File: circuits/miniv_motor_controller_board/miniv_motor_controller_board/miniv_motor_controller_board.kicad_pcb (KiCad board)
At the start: 2 copper layers, 25 parts, among them J1 DC_in, J2 T200_ESC_power, J3 T200_ESC_signal, J4 Conn_EStop_Signal, Q1 2SC1815, Q2 2SC1815, U1 Teensy4.1, U2 TLP624, U3 TLP624

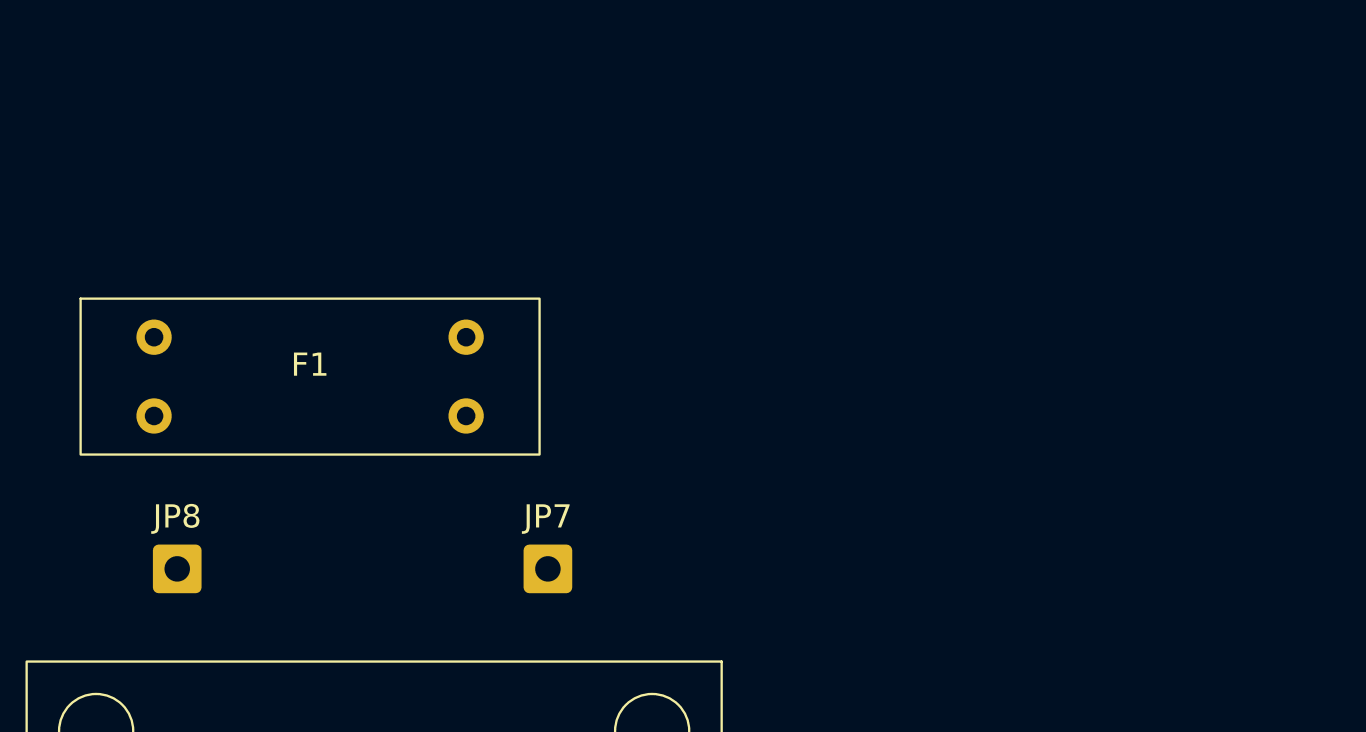
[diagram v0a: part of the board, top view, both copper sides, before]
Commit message: fix connection
Signed-off-by: Masaya Kataoka <ms.kataoka@gmail.com>
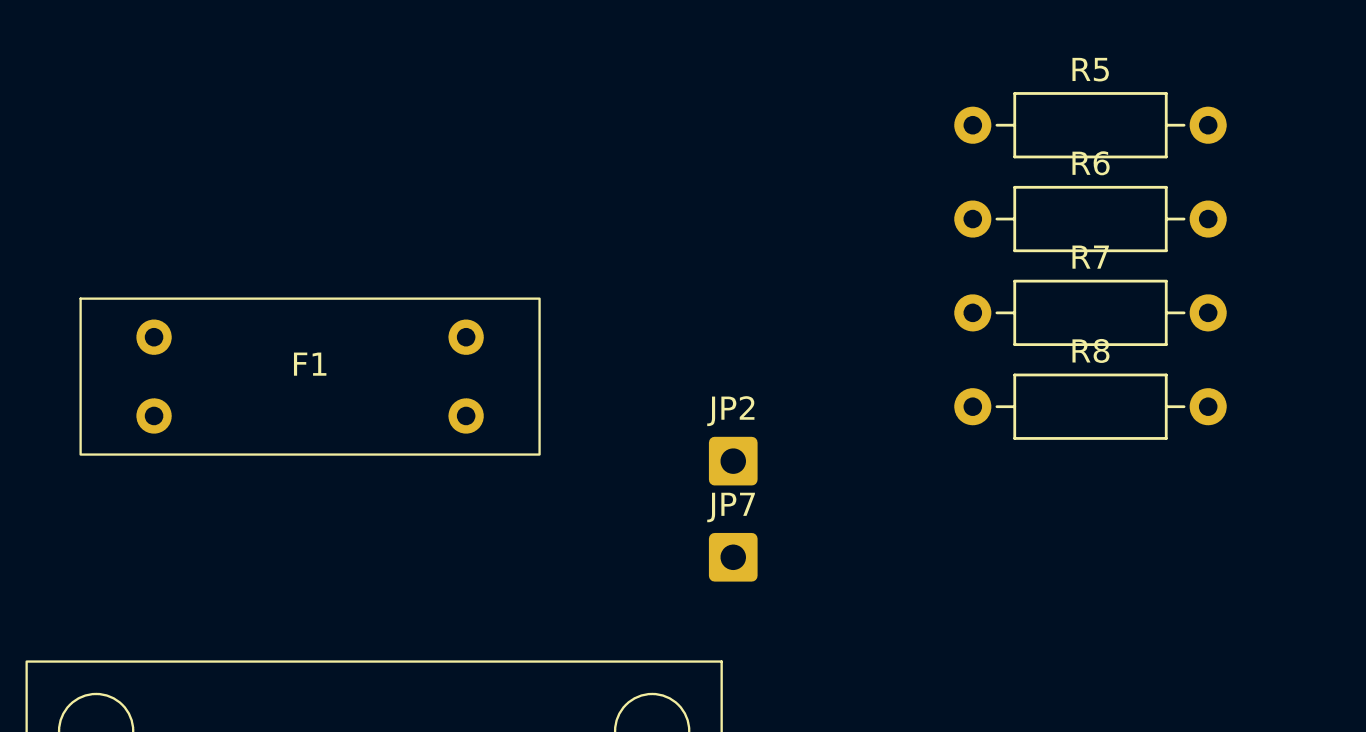
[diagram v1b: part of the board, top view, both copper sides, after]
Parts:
- removed JP8: Jumper_2_Bridged, Connector_Wire:SolderWire-0.5sqmm_1x01_D0.9mm_OD2.1mm
- added JP2: Jumper_2_Bridged, Connector_Wire:SolderWire-0.5sqmm_1x01_D0.9mm_OD2.1mm, F.Cu at (93.0, 48.4)
- added R5: 390, Resistor_THT:R_Axial_DIN0207_L6.3mm_D2.5mm_P10.16mm_Horizontal, F.Cu at (103.3, 33.9)
- added R6: 1K, Resistor_THT:R_Axial_DIN0207_L6.3mm_D2.5mm_P10.16mm_Horizontal, F.Cu at (103.3, 37.9)
- added R7: 1K, Resistor_THT:R_Axial_DIN0207_L6.3mm_D2.5mm_P10.16mm_Horizontal, F.Cu at (103.3, 42.0)
- added R8: 390, Resistor_THT:R_Axial_DIN0207_L6.3mm_D2.5mm_P10.16mm_Horizontal, F.Cu at (103.3, 46.0)
- moved JP7 8.02 mm to (93.0, 52.5)
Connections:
- JP7 pad 1: Net-(JP7-A) -> GND
- U1 pad 45: Net-(U1-23_A9_CRX1_MCLK1) -> Net-(JP1-A)
- U2 pad 1: Net-(JP1-A) -> Net-(R5-Pad2)
- U3 pad 1: Net-(J4-Pin_2) -> Net-(R7-Pad1)
- U3 pad 4: Net-(JP3-B) -> Net-(JP3-A)

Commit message: update text
Signed-off-by: Masaya Kataoka <ms.kataoka@gmail.com>
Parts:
- moved JP7 24.5 mm to (68.5, 53.0)
- moved JP2 12.4 mm to (81.5, 53.0)
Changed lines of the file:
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@@
 	(footprint "Connector_Wire:SolderWire-0.5sqmm_1x01_D0.9mm_OD2.1mm"
 		(layer "F.Cu")
-		(at 93 52.5)
+		(at 68.5 53)
 		(descr "Soldered wire connection, for a single 0.5 mm² wire, basic insulation, conductor diameter 0.9mm, outer diameter 2.1mm, size source Multi-Contact FLEXI-E 0.5 (https://ec.staubli.com/AcroFiles/Catalogues/TM_Cab-Main-11014119_(en)_hi.pdf), bend radius 3 times outer diameter, generated with kicad-footprint-generator")
 		(tags "connector wire 0.5sqmm")
@@
 	(footprint "Connector_Wire:SolderWire-0.5sqmm_1x01_D0.9mm_OD2.1mm"
 		(layer "F.Cu")
-		(at 93 48.35)
+		(at 81.5 53)
 		(descr "Soldered wire connection, for a single 0.5 mm² wire, basic insulation, conductor diameter 0.9mm, outer diameter 2.1mm, size source Multi-Contact FLEXI-E 0.5 (https://ec.staubli.com/AcroFiles/Catalogues/TM_Cab-Main-11014119_(en)_hi.pdf), bend radius 3 times outer diameter, generated with kicad-footprint-generator")
 		(tags "connector wire 0.5sqmm")

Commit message: add hole
Signed-off-by: Masaya Kataoka <ms.kataoka@gmail.com>
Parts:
- removed the R5 at (103.3, 33.9)
- removed the R5 at (102.5, 75.0)
- added H1: MountingHole, MountingHole:MountingHole_3.2mm_M3, F.Cu at (35.0, 130.0)
- added H2: MountingHole, MountingHole:MountingHole_3.2mm_M3, F.Cu at (35.0, 39.0)
- added H3: MountingHole, MountingHole:MountingHole_3.2mm_M3, F.Cu at (104.0, 39.0)
- added H4: MountingHole, MountingHole:MountingHole_3.2mm_M3, F.Cu at (104.0, 130.0)
- added R5: 390, Resistor_THT:R_Axial_DIN0207_L6.3mm_D2.5mm_P10.16mm_Horizontal, F.Cu at (95.5, 107.5)
- J1, J2: footprint Connector_AMASS:AMASS_XT30PW-F_1x02_P2.50mm_Horizontal -> Connector_AMASS:AMASS_XT60PW-F_1x02_P7.20mm_Horizontal
- J4: footprint Connector_AMASS:AMASS_XT30PW-F_1x02_P2.50mm_Horizontal -> Connector_JST:JST_XH_B2B-XH-A_1x02_P2.50mm_Vertical
- JP2: value Jumper_2_Bridged -> Relay_NO
- JP3: value Jumper_EStop -> Disable_EStop
- JP4: value Jumper_2_Bridged -> Relay_SIG
- JP5: value Jumper_2_Bridged -> Relay_GND
- JP6: value Jumper_2_Bridged -> Relay_VCC
- JP7: value Jumper_2_Bridged -> Relay_COM
- moved R7 100.4 mm to (33.5, 114.1), turned to 90 degrees
- moved R8 89.0 mm to (33.5, 101.2), turned to 90 degrees
- moved R6 56.6 mm to (95.5, 93.9), turned to -90 degrees
- moved D2 56.3 mm to (79.0, 120.0), turned to 0 degrees
- moved J1 46.0 mm to (37.5, 70.5)
- moved J3 45.2 mm to (92.0, 51.6), turned to 0 degrees
- moved JP7 44.9 mm to (38.0, 86.0)
- moved JP6 32.9 mm to (38.0, 101.0)
- moved R4 30.4 mm to (84.0, 120.0), turned to 0 degrees
- moved R2 20.4 mm to (98.0, 122.1), turned to 90 degrees
- moved R3 19.7 mm to (83.9, 125.0)
- moved M78AR05-1 19.3 mm to (70.0, 121.0), turned to 180 degrees
- moved R1 14.1 mm to (75.5, 132.5)
- moved Q1 13.8 mm to (81.0, 129.5)
- moved Q2 13.8 mm to (88.5, 129.5)
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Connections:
- JP7 pad 1: GND -> +12V
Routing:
- net GND: track 0.00 -> 239.5 mm
- net Net-(JP3-A): track 0.00 -> 107.8 mm
- net +12V: track 0.00 -> 79.8 mm
- net Net-(JP1-A): track 0.00 -> 64.6 mm
- net Net-(JP3-B): track 0.00 -> 55.0 mm
- net Net-(J2-Pin_2): track 0.00 -> 35.8 mm
- net Net-(JP4-A): track 0.00 -> 34.5 mm
- net Net-(J4-Pin_2): track 0.00 -> 33.1 mm
- net Net-(J3-Pin_2): track 0.00 -> 29.7 mm
- net Net-(R5-Pad2): track 0.00 -> 29.3 mm
- net Net-(R7-Pad1): track 0.00 -> 22.3 mm
- net Net-(Q2-B): track 0.00 -> 14.4 mm
- net Net-(R1-Pad2): track 0.00 -> 14.3 mm
- net Net-(J4-Pin_1): track 0.00 -> 13.3 mm
- net Net-(Q1-B): track 0.00 -> 5.71 mm
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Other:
- board outline added: 78 x 102 mm

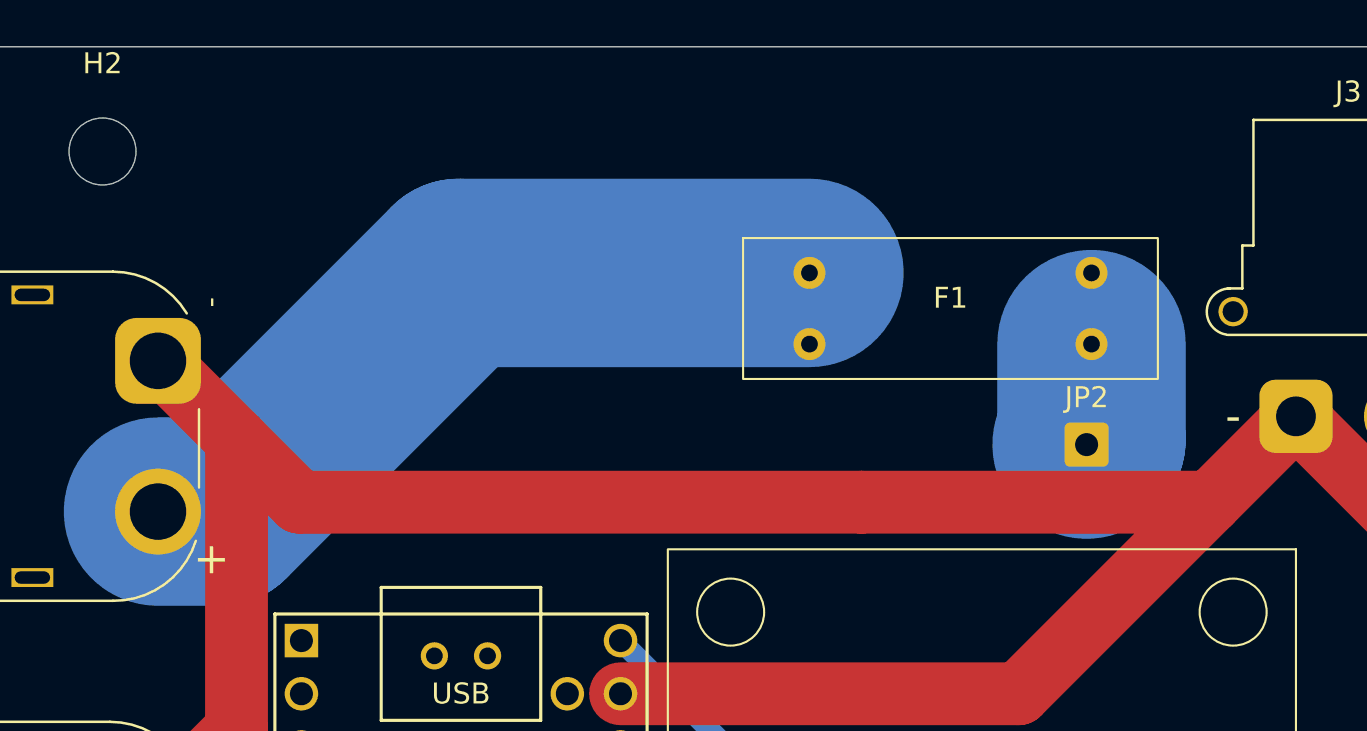
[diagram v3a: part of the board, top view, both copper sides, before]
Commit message: add RJ45 connector
Signed-off-by: Masaya Kataoka <ms.kataoka@gmail.com>
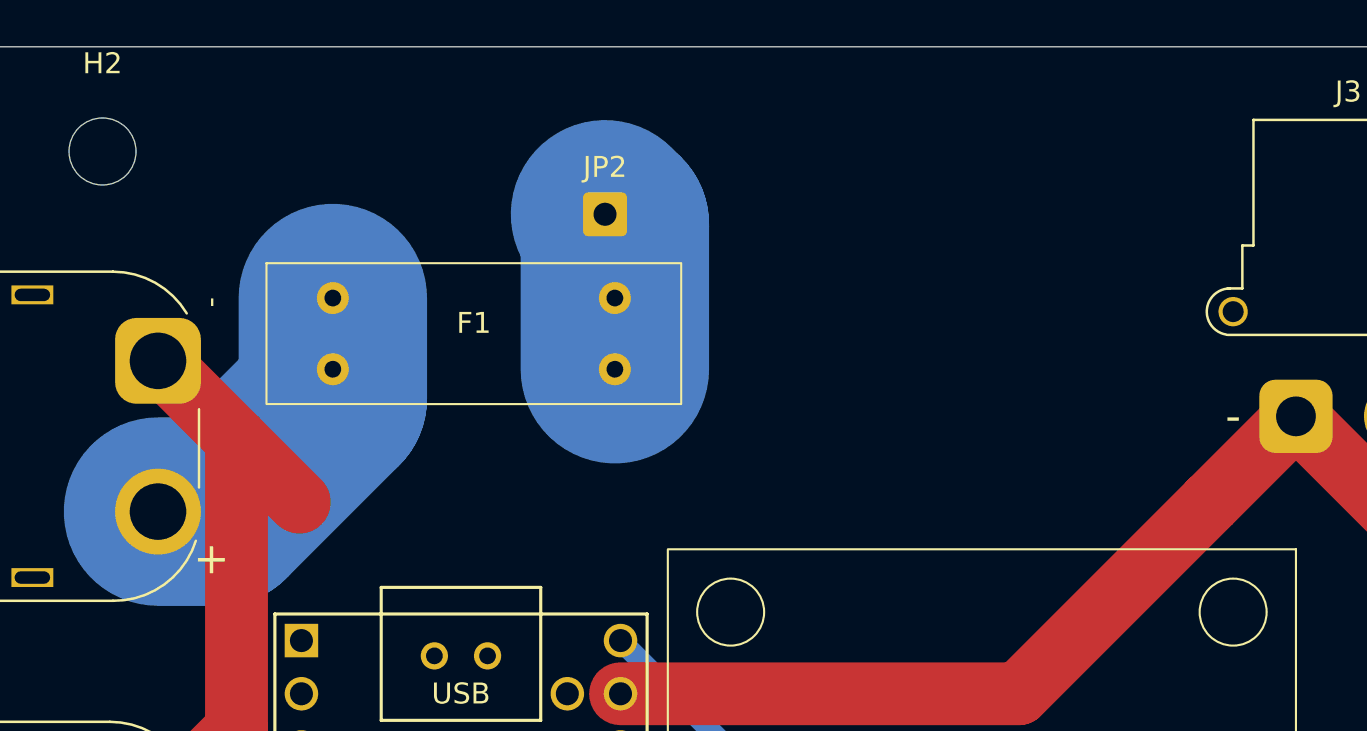
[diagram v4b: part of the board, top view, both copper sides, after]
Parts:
- moved JP2 25.5 mm to (59.0, 42.0)
- moved F1 22.8 mm to (52.7, 47.7)
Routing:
- net GND: track 239.5 -> 196.0 mm
- net Net-(J2-Pin_2): track 35.8 -> 15.4 mm
- net Net-(JP2-A): track 4.90 -> 7.59 mm
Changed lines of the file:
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@@
 		(tags "Resistor Axial_DIN0207 series Axial Horizontal pin pitch 10.16mm 0.25W = 1/4W length 6.3mm diameter 2.5mm")
 		(property "Reference" "R4"
-			(at 8.08 2.5 360)
+			(at 8.08 2.5 0)
 			(layer "F.SilkS")
 			(effects
@@
 		)
 		(property "Value" "470"
-			(at 5.08 2.37 360)
+			(at 5.08 2.37 0)
 			(layer "F.Fab")
 			(effects
@@
 		)
 		(fp_text user "${REFERENCE}"
-			(at 5.08 0 360)
+			(at 5.08 0 0)
 			(layer "F.Fab")
 			(effects
@@
 	(footprint "Connector_Wire:SolderWire-0.5sqmm_1x01_D0.9mm_OD2.1mm"
 		(layer "F.Cu")
-		(at 82 53)
+		(at 59 42)
 		(descr "Soldered wire connection, for a single 0.5 mm² wire, basic insulation, conductor diameter 0.9mm, outer diameter 2.1mm, size source Multi-Contact FLEXI-E 0.5 (https://ec.staubli.com/AcroFiles/Catalogues/TM_Cab-Main-11014119_(en)_hi.pdf), bend radius 3 times outer diameter, generated with kicad-footprint-generator")
 		(tags "connector wire 0.5sqmm")
@@
 	(footprint "3557-15:3557-15"
 		(layer "F.Cu")
-		(at 75.5 46.5)
+		(at 52.735 47.7)
 		(property "Reference" "F1"
 			(at 0 -0.5 0)
@@
 	)
 	(segment
-		(start 71.25 55.75)
-		(end 44.4 55.75)
-		(width 3)
-		(layer "F.Cu")
-		(net 2)
-	)
-	(segment
 		(start 83.92 124.92)
 		(end 79 120)
@@
 	)
 	(segment
-		(start 71.25 55.75)
-		(end 87.9 55.75)
-		(width 3)
-		(layer "F.Cu")
-		(net 2)
-	)
-	(segment
 		(start 44.4 55.75)
 		(end 41.4 52.75)
@@
 	)
 	(segment
-		(start 68.765 44.8)
-		(end 52.003388 44.8)
+		(start 40.603388 56.2)
+		(end 37.65 56.2)
 		(width 9)
 		(layer "B.Cu")
@@
 	)
 	(segment
-		(start 40.603388 56.2)
-		(end 37.65 56.2)
+		(start 46 50.803388)
+		(end 46 46)
 		(width 9)
 		(layer "B.Cu")
@@
 	)
 	(segment
-		(start 52.003388 44.8)
-		(end 40.603388 56.2)
+		(start 40.603388 56.2)
+		(end 46 50.803388)
 		(width 9)
 		(layer "B.Cu")
@@
 	)
 	(segment
-		(start 82.235 48.2)
-		(end 82.235 52.765)
+		(start 59.47 49.4)
+		(end 59.47 42.47)
 		(width 9)
 		(layer "B.Cu")
@@
 	)
 	(segment
-		(start 82.235 52.765)
-		(end 82 53)
+		(start 59.47 42.47)
+		(end 59 42)
 		(width 9)
 		(layer "B.Cu")

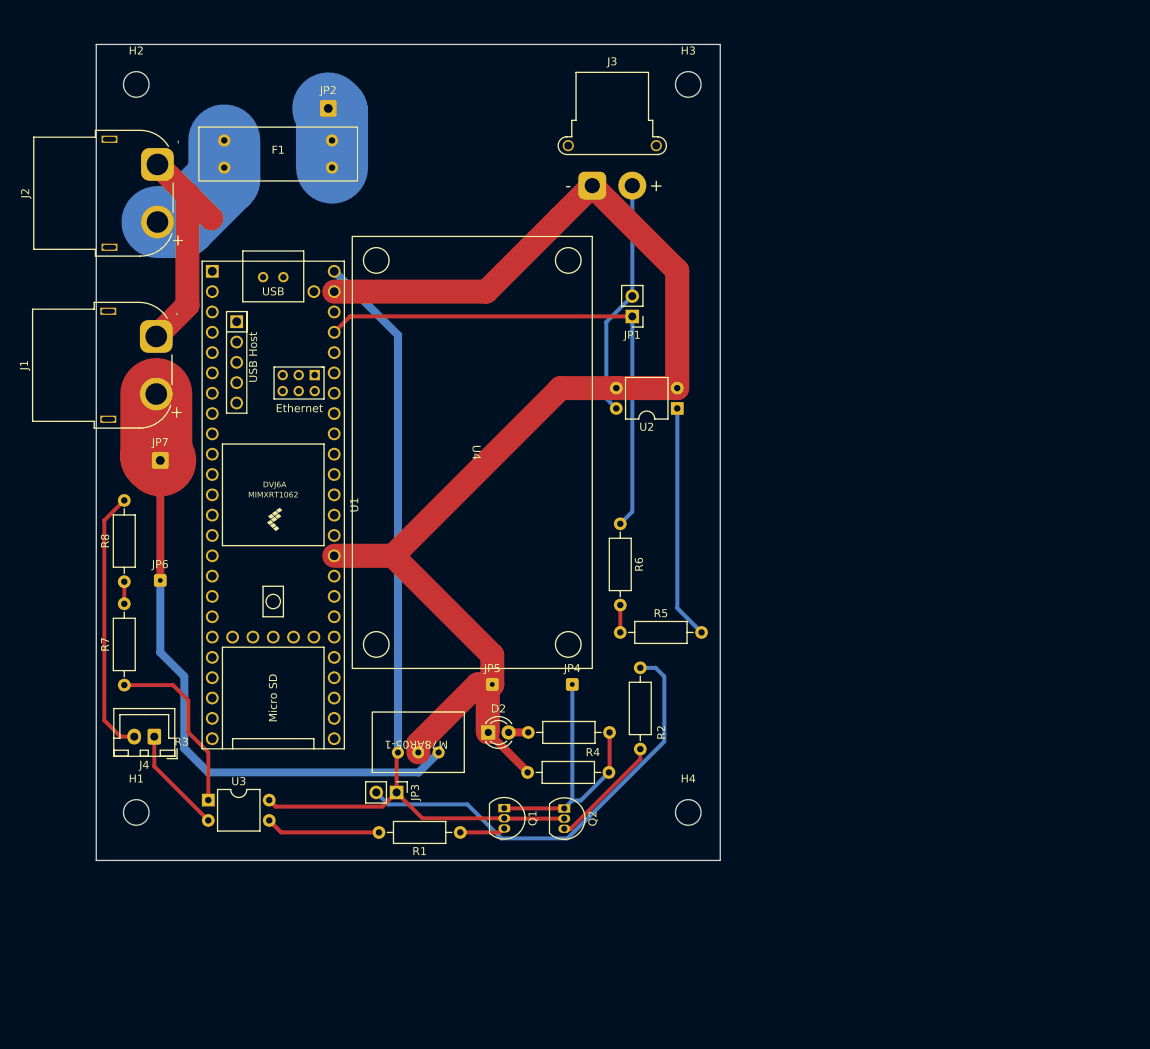
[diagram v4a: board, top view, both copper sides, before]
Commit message: add SS-12D00G3 and modify RJLD-260YC1
Signed-off-by: Masaya Kataoka <ms.kataoka@gmail.com>
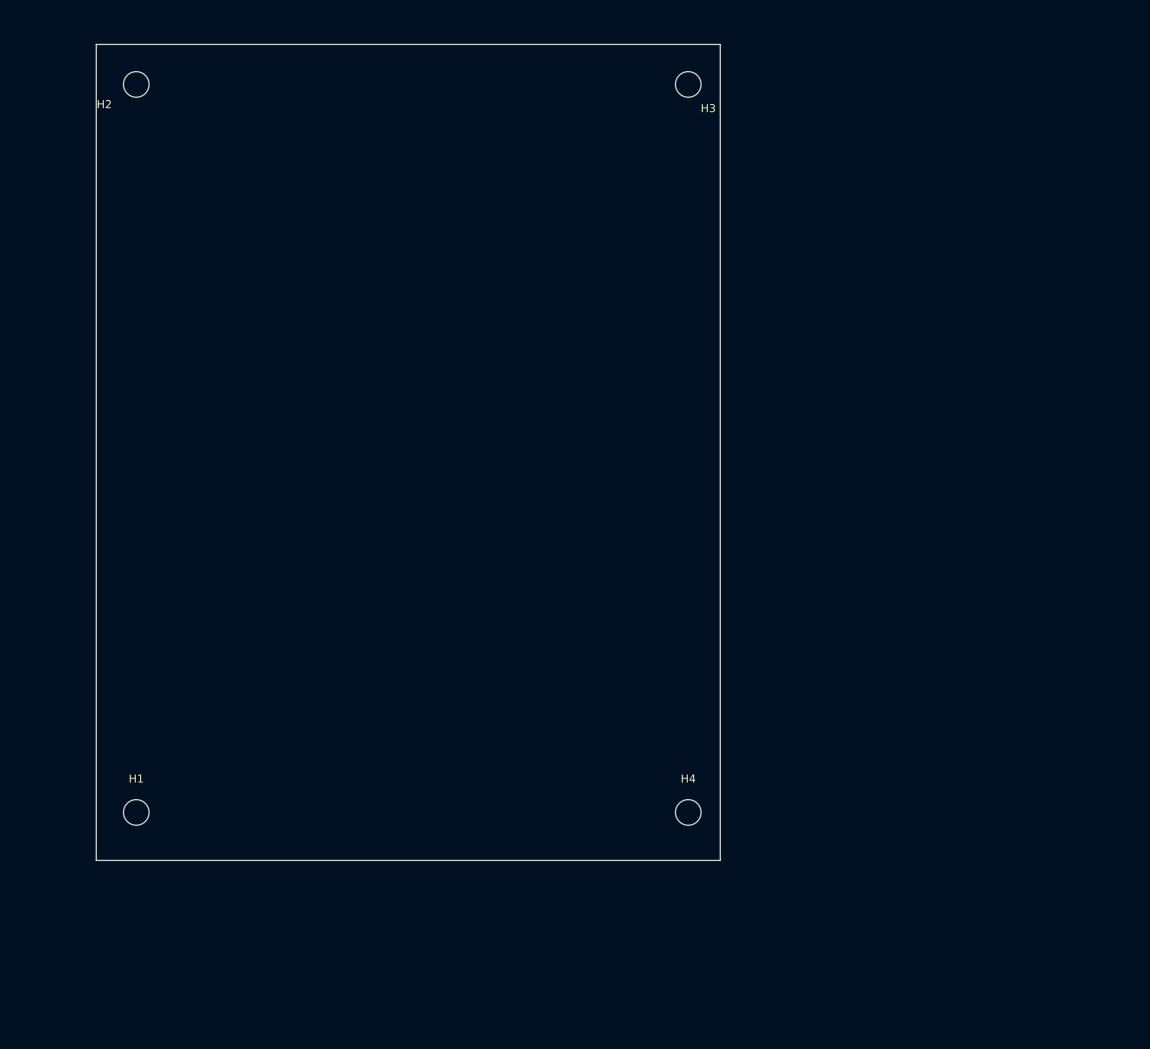
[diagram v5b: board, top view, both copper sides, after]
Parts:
- removed D2: LED, LED_THT:LED_D3.0mm
- removed F1: Fuse, 3557-15:3557-15
- removed J1: DC_in, Connector_AMASS:AMASS_XT60PW-F_1x02_P7.20mm_Horizontal
- removed J2: T200_ESC_power, Connector_AMASS:AMASS_XT60PW-F_1x02_P7.20mm_Horizontal
- removed J3: T200_ESC_signal, Connector_AMASS:AMASS_XT30PW-F_1x02_P2.50mm_Horizontal
- removed J4: Conn_EStop_Signal, Connector_JST:JST_XH_B2B-XH-A_1x02_P2.50mm_Vertical
- removed JP1: Jumper_2_Open, Connector_PinHeader_2.54mm:PinHeader_1x02_P2.54mm_Vertical
- removed JP2: Relay_NO, Connector_Wire:SolderWire-0.5sqmm_1x01_D0.9mm_OD2.1mm
- removed JP3: Disable_EStop, Connector_PinHeader_2.54mm:PinHeader_1x02_P2.54mm_Vertical
- removed JP4: Relay_SIG, Connector_Wire:SolderWire-0.1sqmm_1x01_D0.4mm_OD1mm
- removed JP5: Relay_GND, Connector_Wire:SolderWire-0.1sqmm_1x01_D0.4mm_OD1mm
- removed JP6: Relay_VCC, Connector_Wire:SolderWire-0.1sqmm_1x01_D0.4mm_OD1mm
- removed JP7: Relay_COM, Connector_Wire:SolderWire-0.5sqmm_1x01_D0.9mm_OD2.1mm
- removed M78AR05-1: ~, M78AR05-1:M78AR05-1
- removed Q1, Q2: 2SC1815, Package_TO_SOT_THT:TO-92_Inline
- removed R1, R2: 100k, Resistor_THT:R_Axial_DIN0207_L6.3mm_D2.5mm_P10.16mm_Horizontal
- removed R3, R6, R7: 1K, Resistor_THT:R_Axial_DIN0207_L6.3mm_D2.5mm_P10.16mm_Horizontal
- removed R4: 470, Resistor_THT:R_Axial_DIN0207_L6.3mm_D2.5mm_P10.16mm_Horizontal
- removed R5, R8: 390, Resistor_THT:R_Axial_DIN0207_L6.3mm_D2.5mm_P10.16mm_Horizontal
- removed U1: Teensy4.1, Teensy:Teensy41
- removed U2, U3: TLP624, Package_DIP:DIP-4_W7.62mm
- removed U4: ~, AE-RELAY953B-12V:AE-RELAY953B-12V
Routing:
- net GND: track 196.0 -> 0.00 mm
- net Net-(JP3-A): track 107.8 -> 0.00 mm
- net +12V: track 79.8 -> 0.00 mm
- net Net-(JP1-A): track 64.6 -> 0.00 mm
- net Net-(JP3-B): track 55.0 -> 0.00 mm
- net Net-(JP4-A): track 34.5 -> 0.00 mm
- net Net-(J4-Pin_2): track 33.1 -> 0.00 mm
- net Net-(J3-Pin_2): track 29.7 -> 0.00 mm
- net Net-(R5-Pad2): track 29.3 -> 0.00 mm
- net Net-(R7-Pad1): track 22.3 -> 0.00 mm
- net Net-(J2-Pin_2): track 15.4 -> 0.00 mm
- net Net-(Q2-B): track 14.4 -> 0.00 mm
- net Net-(R1-Pad2): track 14.3 -> 0.00 mm
- net Net-(J4-Pin_1): track 13.3 -> 0.00 mm
- net Net-(JP2-A): track 7.59 -> 0.00 mm
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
